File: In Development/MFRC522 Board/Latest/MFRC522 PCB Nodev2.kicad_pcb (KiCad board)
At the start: 2 copper layers, 120 x 50 mm, 46 parts, among them P1 ESP32 NODEMCU DEVKIT1 LEFT HE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, P2 ESP32 NODEMCU DEVKIT1 RIGHT H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, Q2 Q_NPN_BEC, U1 MFRC522, Y1 27.12 MHz

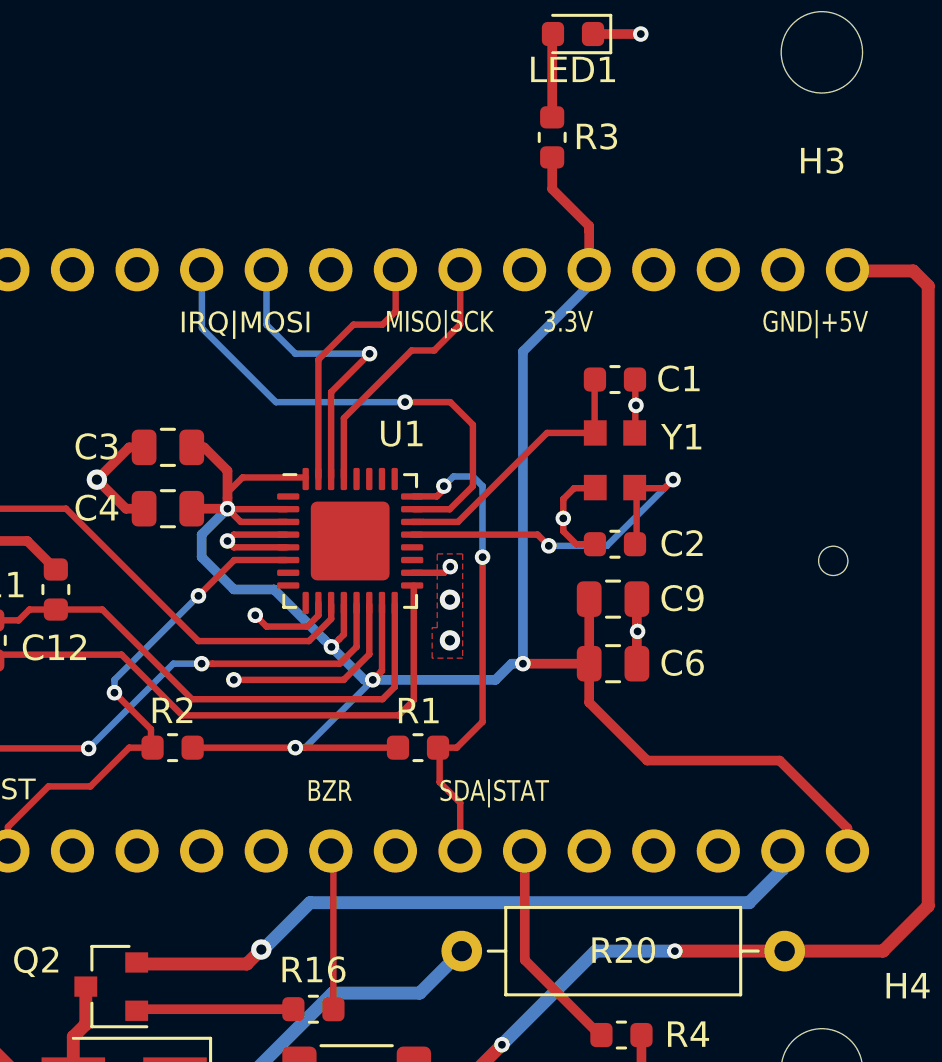
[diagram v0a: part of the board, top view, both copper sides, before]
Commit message: update for ESP32, so not actually Node anymore
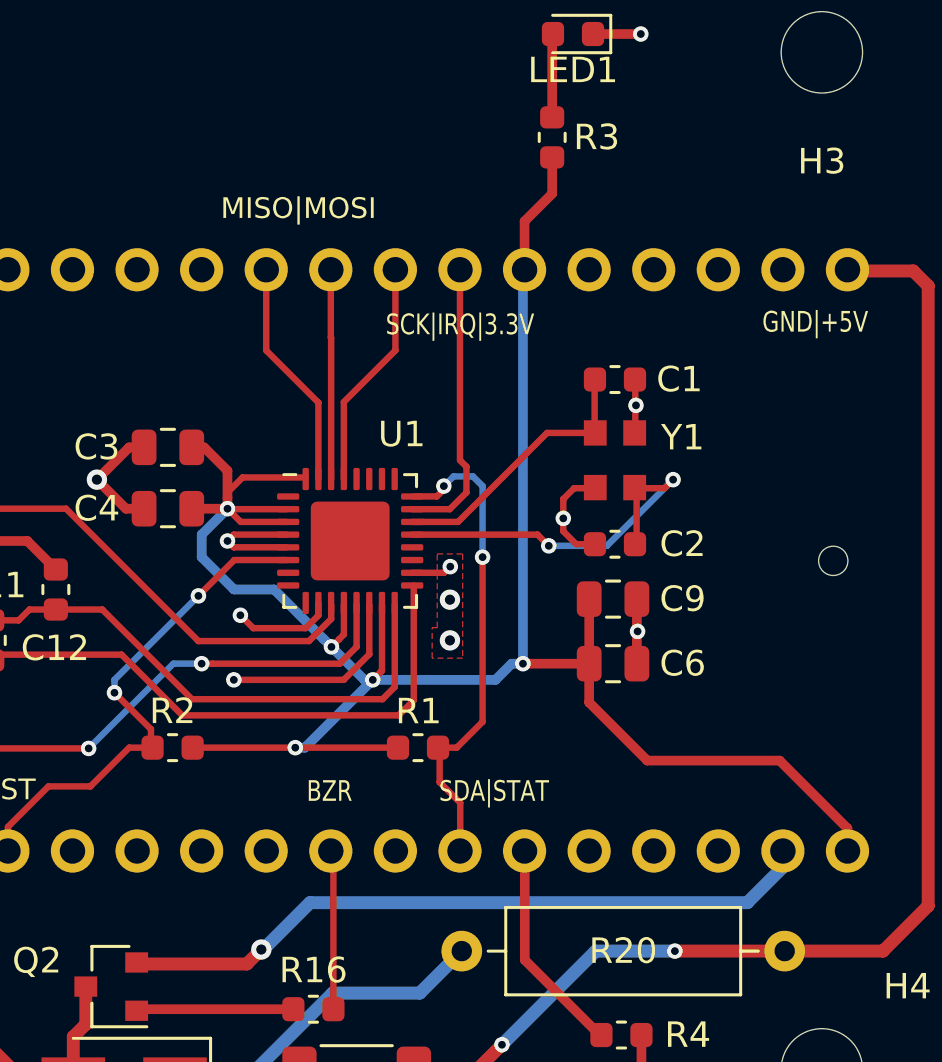
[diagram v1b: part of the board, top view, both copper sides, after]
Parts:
- R3: value 15 -> 24
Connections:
- P1 pad 10: Net-(P1-Pad10) -> +3V3
- P1 pad 11: +3V3 -> Net-(P1-Pad11)
- P1 pad 5: /IRQ -> Net-(P1-Pad5)
- P1 pad 6: /MOSI -> /MISO
- P1 pad 7: Net-(P1-Pad7) -> /MOSI
- P1 pad 8: /MISO -> /SCK
- P1 pad 9: /SCK -> /IRQ
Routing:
- net /IRQ: track 19.6 -> 11.3 mm, vias 1 -> 0
- net /MOSI: track 12.1 -> 8.24 mm, vias 1 -> 0
- net +3V3: track 90.0 -> 88.1 mm
- net /SCK: track 10.5 -> 9.07 mm
- net Net-(P1-Pad11): track 0.00 -> 1.28 mm
- net /MISO: track 10.0 -> 9.08 mm
- net GND: track 859.8 -> 860.4 mm
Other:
- board text added: "MISO|MOSI"
- board text added: "SCK|IRQ|3.3V"
- board text removed: "IRQ|MOSI"
- board text removed: "MISO|SCK 3.3V"

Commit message: upd esp32
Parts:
- added H3: MountingHole, MountingHole:MountingHole_3.2mm_M3, F.Cu at (111.6, 62.7)
- moved R3 4.90 mm to (137.5, 62.0), turned to 0 degrees
- moved P1 2.54 mm to (116.3, 68.7)
- moved H7 1.29 mm to (151.3, 81.4)
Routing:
- net +3V3: track 88.1 -> 96.1 mm
- net /IRQ: track 11.3 -> 13.8 mm
- net /SCK: track 9.07 -> 11.6 mm
- net /MOSI: track 8.24 -> 10.8 mm
- net /MISO: track 9.08 -> 11.6 mm
- net +5V: track 50.9 -> 52.5 mm
- net Net-(LED1-Pad2): track 3.29 -> 2.01 mm
- net Net-(P1-Pad11): track 1.28 -> 0.00 mm
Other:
- board text added: "ESP32 Goes Here"
- board text removed: "NodeMCU Here"
